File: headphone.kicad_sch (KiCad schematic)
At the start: 5 parts, among them J4 SFV14R-2STE1HLF, Q2 NTK3139PT1G

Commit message: layout, routing: relayout and reroute board
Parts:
- J4: value SFV14R-2STE1HLF -> (none); footprint Gigahawk:SFV14R2STE1HLF -> (none)
- Q2: value NTK3139PT1G -> (none); footprint Package_TO_SOT_SMD:SOT-723 -> (none)
- R28, R30: value 10k -> (none); footprint Resistor_SMD:R_0402_1005Metric -> (none)
- R29: value DNI -> (none); footprint Resistor_SMD:R_0402_1005Metric -> (none)
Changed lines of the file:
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@@
     (in_bom yes) (on_board yes) (fields_autoplaced)
     (property "Reference" "Q2" (id 0) (at 181.865 95.25 90))
-    (property "Value" "NTK3139PT1G" (id 1) (at 181.865 97.79 90))
-    (property "Footprint" "Package_TO_SOT_SMD:SOT-723" (id 2) (at 193.04 104.14 0)
+    (property "Value" "" (id 1) (at 181.865 97.79 90))
+    (property "Footprint" "" (id 2) (at 193.04 104.14 0)
       (effects (font (size 1.27 1.27)) hide)
     )
@@
     (in_bom yes) (on_board yes)
     (property "Reference" "R30" (id 0) (at 186.69 113.665 90))
-    (property "Value" "10k" (id 1) (at 186.69 115.57 90))
-    (property "Footprint" "Resistor_SMD:R_0402_1005Metric" (id 2) (at 186.69 111.76 0)
+    (property "Value" "" (id 1) (at 186.69 115.57 90))
+    (property "Footprint" "" (id 2) (at 186.69 111.76 0)
       (effects (font (size 1.27 1.27)) hide)
     )
@@
     (in_bom yes) (on_board yes) (fields_autoplaced)
     (property "Reference" "J4" (id 0) (at 119.38 93.98 0))
-    (property "Value" "SFV14R-2STE1HLF" (id 1) (at 119.38 96.52 0))
-    (property "Footprint" "Gigahawk:SFV14R2STE1HLF" (id 2) (at 127 99.06 0)
+    (property "Value" "" (id 1) (at 119.38 96.52 0))
+    (property "Footprint" "" (id 2) (at 127 99.06 0)
       (effects (font (size 1.27 1.27)) (justify left) hide)
     )
@@
     (in_bom yes) (on_board yes)
     (property "Reference" "R29" (id 0) (at 179.07 113.665 90))
-    (property "Value" "DNI" (id 1) (at 179.07 115.57 90))
-    (property "Footprint" "Resistor_SMD:R_0402_1005Metric" (id 2) (at 179.07 111.76 0)
+    (property "Value" "" (id 1) (at 179.07 115.57 90))
+    (property "Footprint" "" (id 2) (at 179.07 111.76 0)
       (effects (font (size 1.27 1.27)) hide)
     )
@@
       (effects (font (size 1.27 1.27)) (justify left))
     )
-    (property "Value" "10k" (id 1) (at 156.845 110.49 90)
-      (effects (font (size 1.27 1.27)) (justify right))
-    )
-    (property "Footprint" "Resistor_SMD:R_0402_1005Metric" (id 2) (at 154.94 109.22 0)
-      (effects (font (size 1.27 1.27)) hide)
-    )
+    (property "Value" "" (id 1) (at 156.845 110.49 90)
+      (effects (font (size 1.27 1.27)) (justify right))
+    )
+    (property "Footprint" "" (id 2) (at 154.94 109.22 0)
+      (effects (font (size 1.27 1.27)) hide)
+    )

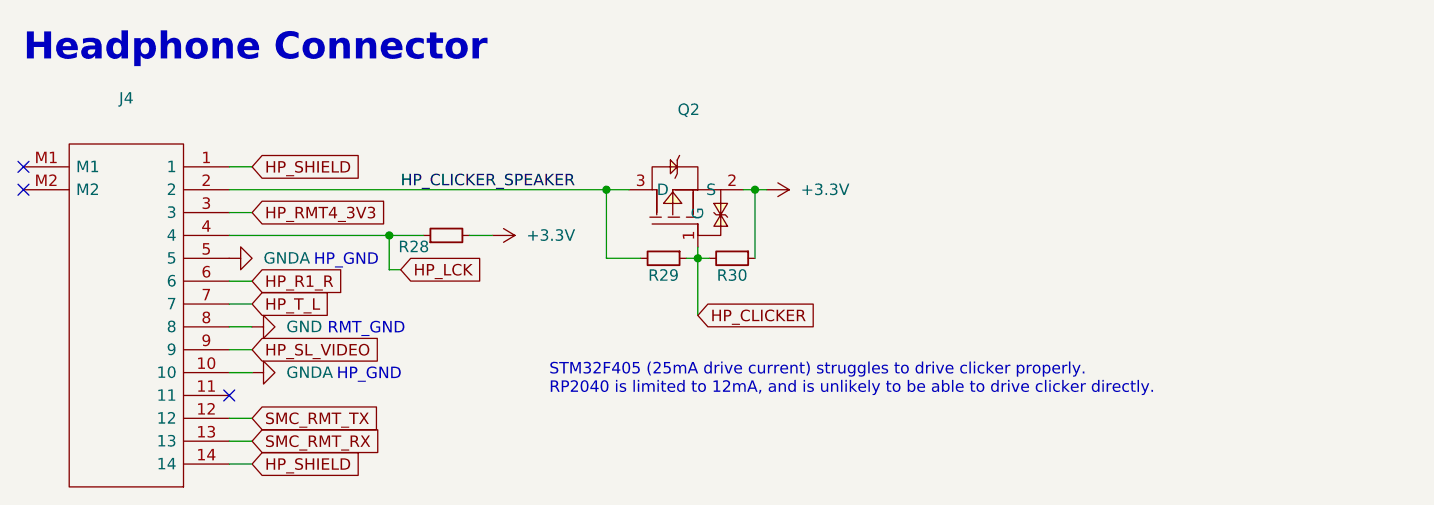
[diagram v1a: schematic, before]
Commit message: layout: add testpoints, extra mounting hole, grounding clips
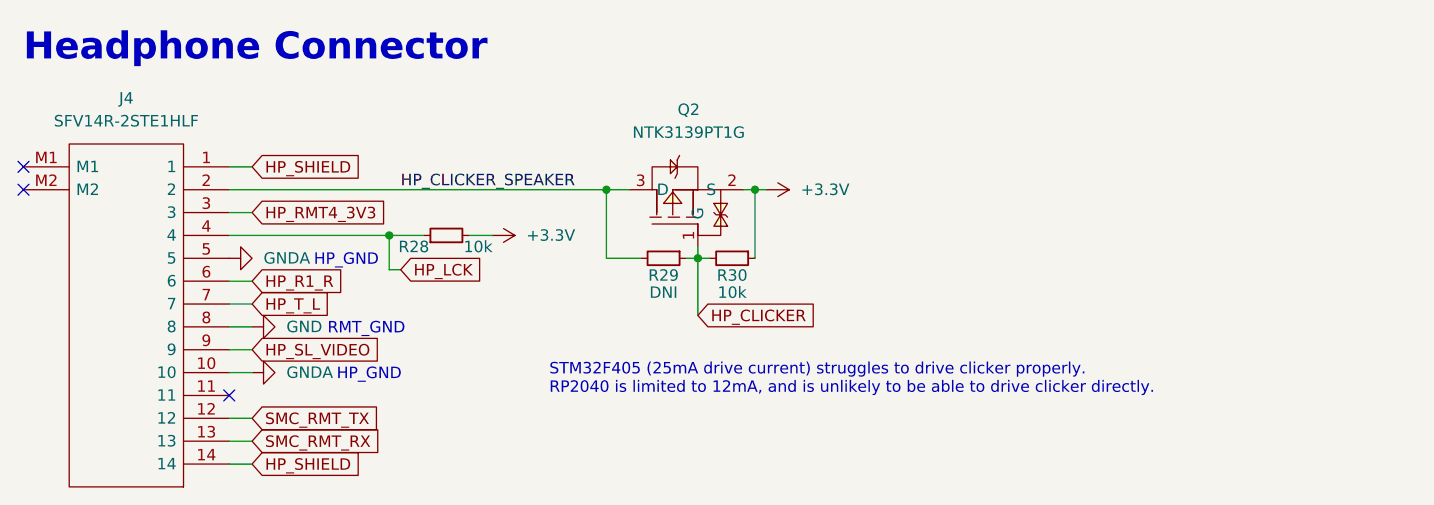
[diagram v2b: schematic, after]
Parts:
- J4: value (none) -> SFV14R-2STE1HLF; footprint (none) -> Gigahawk:SFV14R2STE1HLF
- Q2: value (none) -> NTK3139PT1G; footprint (none) -> Package_TO_SOT_SMD:SOT-723
- R28, R30: value (none) -> 10k; footprint (none) -> Resistor_SMD:R_0402_1005Metric
- R29: value (none) -> DNI; footprint (none) -> Resistor_SMD:R_0402_1005Metric
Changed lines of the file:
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@@
     (in_bom yes) (on_board yes) (fields_autoplaced)
     (property "Reference" "Q2" (id 0) (at 181.865 95.25 90))
-    (property "Value" "" (id 1) (at 181.865 97.79 90))
-    (property "Footprint" "" (id 2) (at 193.04 104.14 0)
+    (property "Value" "NTK3139PT1G" (id 1) (at 181.865 97.79 90))
+    (property "Footprint" "Package_TO_SOT_SMD:SOT-723" (id 2) (at 193.04 104.14 0)
       (effects (font (size 1.27 1.27)) hide)
     )
@@
     (in_bom yes) (on_board yes)
     (property "Reference" "R30" (id 0) (at 186.69 113.665 90))
-    (property "Value" "" (id 1) (at 186.69 115.57 90))
-    (property "Footprint" "" (id 2) (at 186.69 111.76 0)
+    (property "Value" "10k" (id 1) (at 186.69 115.57 90))
+    (property "Footprint" "Resistor_SMD:R_0402_1005Metric" (id 2) (at 186.69 111.76 0)
       (effects (font (size 1.27 1.27)) hide)
     )
@@
     (in_bom yes) (on_board yes) (fields_autoplaced)
     (property "Reference" "J4" (id 0) (at 119.38 93.98 0))
-    (property "Value" "" (id 1) (at 119.38 96.52 0))
-    (property "Footprint" "" (id 2) (at 127 99.06 0)
+    (property "Value" "SFV14R-2STE1HLF" (id 1) (at 119.38 96.52 0))
+    (property "Footprint" "Gigahawk:SFV14R2STE1HLF" (id 2) (at 127 99.06 0)
       (effects (font (size 1.27 1.27)) (justify left) hide)
     )
@@
     (in_bom yes) (on_board yes)
     (property "Reference" "R29" (id 0) (at 179.07 113.665 90))
-    (property "Value" "" (id 1) (at 179.07 115.57 90))
-    (property "Footprint" "" (id 2) (at 179.07 111.76 0)
+    (property "Value" "DNI" (id 1) (at 179.07 115.57 90))
+    (property "Footprint" "Resistor_SMD:R_0402_1005Metric" (id 2) (at 179.07 111.76 0)
       (effects (font (size 1.27 1.27)) hide)
     )
@@
       (effects (font (size 1.27 1.27)) (justify left))
     )
-    (property "Value" "" (id 1) (at 156.845 110.49 90)
-      (effects (font (size 1.27 1.27)) (justify right))
-    )
-    (property "Footprint" "" (id 2) (at 154.94 109.22 0)
-      (effects (font (size 1.27 1.27)) hide)
-    )
+    (property "Value" "10k" (id 1) (at 156.845 110.49 90)
+      (effects (font (size 1.27 1.27)) (justify right))
+    )
+    (property "Footprint" "Resistor_SMD:R_0402_1005Metric" (id 2) (at 154.94 109.22 0)
+      (effects (font (size 1.27 1.27)) hide)
+    )

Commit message: ci: prepare files for CI
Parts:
- Q2: footprint Package_TO_SOT_SMD:SOT-723 -> Gigahawk:SOT-723
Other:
- title: (none) -> piPod IO/SMC Board
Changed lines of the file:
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@@
 (kicad_sch (version 20211123) (generator eeschema)
   (paper "A4")
+  (title_block
+    (title "piPod IO/SMC Board")
+    (date "${DATE}")
+    (rev "%{TAG} (${REVISION})")
+  )
   (junction (at 148.59 109.22) (diameter 0) (color 0 0 0 0)
   )
@@
     (property "Reference" "Q2" (id 0) (at 181.865 95.25 90))
     (property "Value" "NTK3139PT1G" (id 1) (at 181.865 97.79 90))
-    (property "Footprint" "Package_TO_SOT_SMD:SOT-723" (id 2) (at 193.04 104.14 0)
+    (property "Footprint" "Gigahawk:SOT-723" (id 2) (at 193.04 104.14 0)
       (effects (font (size 1.27 1.27)) hide)
     )

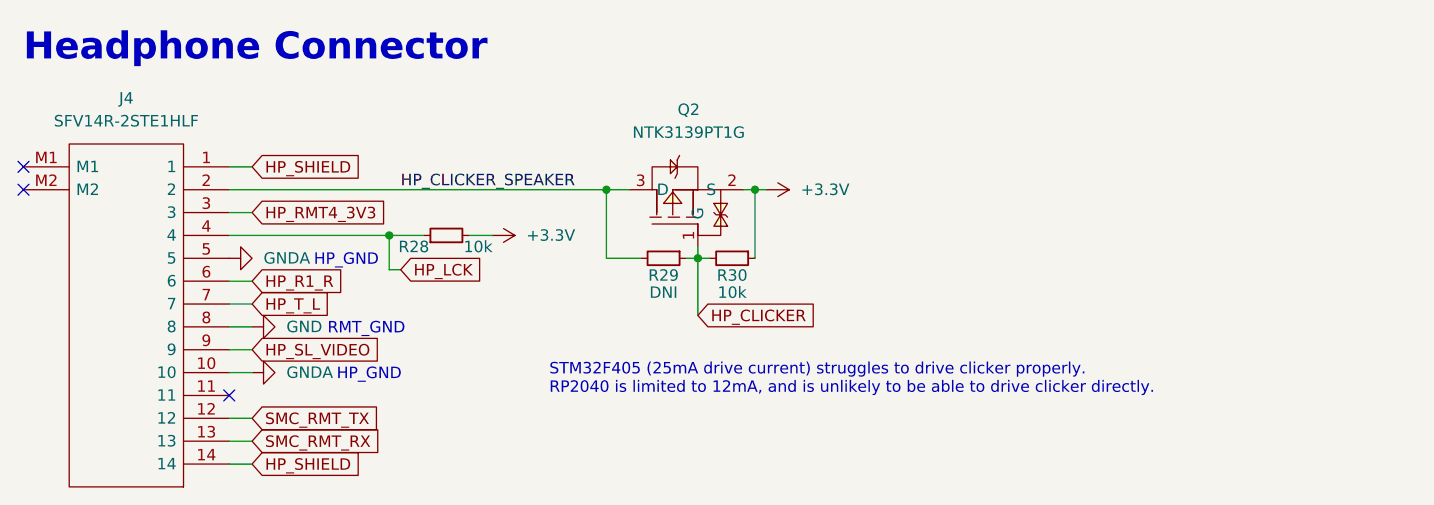
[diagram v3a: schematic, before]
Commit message: ci: test marking parts in sch for bom
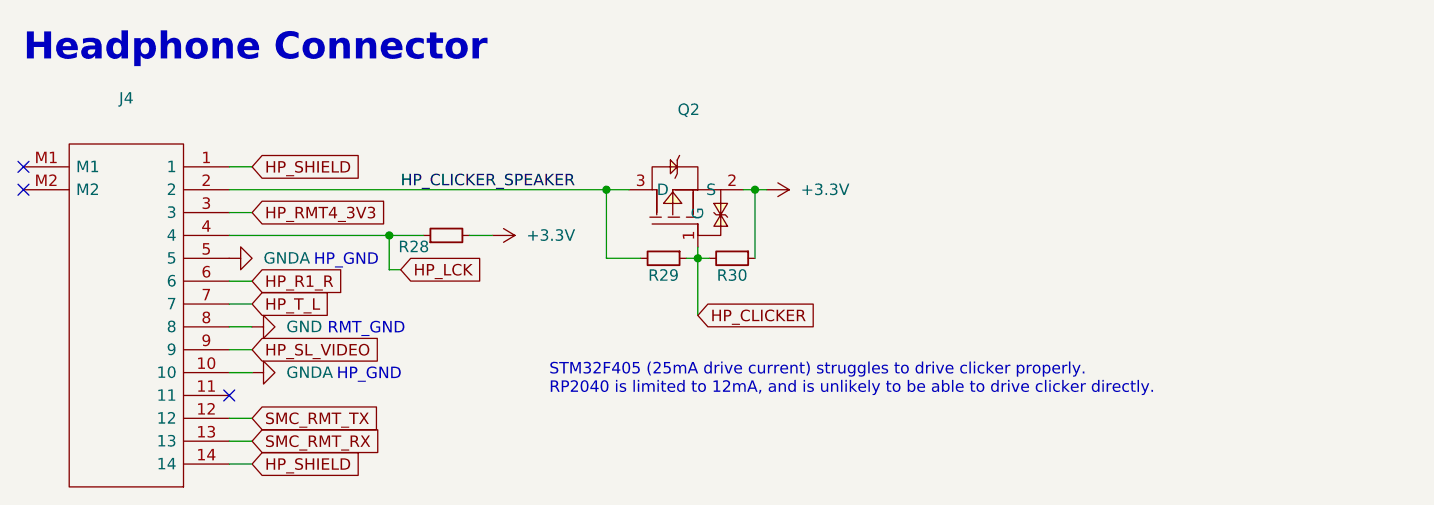
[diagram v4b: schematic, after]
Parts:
- J4: value SFV14R-2STE1HLF -> (none); footprint Gigahawk:SFV14R2STE1HLF -> (none)
- Q2: value NTK3139PT1G -> (none); footprint Gigahawk:SOT-723 -> (none)
- R28, R30: value 10k -> (none); footprint Resistor_SMD:R_0402_1005Metric -> (none)
- R29: value DNI -> (none); footprint Resistor_SMD:R_0402_1005Metric -> (none)
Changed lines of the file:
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@@
     (in_bom yes) (on_board yes) (fields_autoplaced)
     (property "Reference" "Q2" (id 0) (at 181.865 95.25 90))
-    (property "Value" "NTK3139PT1G" (id 1) (at 181.865 97.79 90))
-    (property "Footprint" "Gigahawk:SOT-723" (id 2) (at 193.04 104.14 0)
+    (property "Value" "" (id 1) (at 181.865 97.79 90))
+    (property "Footprint" "" (id 2) (at 193.04 104.14 0)
       (effects (font (size 1.27 1.27)) hide)
     )
@@
     (in_bom yes) (on_board yes)
     (property "Reference" "R30" (id 0) (at 186.69 113.665 90))
-    (property "Value" "10k" (id 1) (at 186.69 115.57 90))
-    (property "Footprint" "Resistor_SMD:R_0402_1005Metric" (id 2) (at 186.69 111.76 0)
+    (property "Value" "" (id 1) (at 186.69 115.57 90))
+    (property "Footprint" "" (id 2) (at 186.69 111.76 0)
       (effects (font (size 1.27 1.27)) hide)
     )
@@
     (in_bom yes) (on_board yes) (fields_autoplaced)
     (property "Reference" "J4" (id 0) (at 119.38 93.98 0))
-    (property "Value" "SFV14R-2STE1HLF" (id 1) (at 119.38 96.52 0))
-    (property "Footprint" "Gigahawk:SFV14R2STE1HLF" (id 2) (at 127 99.06 0)
+    (property "Value" "" (id 1) (at 119.38 96.52 0))
+    (property "Footprint" "" (id 2) (at 127 99.06 0)
       (effects (font (size 1.27 1.27)) (justify left) hide)
     )
@@
     (in_bom yes) (on_board yes)
     (property "Reference" "R29" (id 0) (at 179.07 113.665 90))
-    (property "Value" "DNI" (id 1) (at 179.07 115.57 90))
-    (property "Footprint" "Resistor_SMD:R_0402_1005Metric" (id 2) (at 179.07 111.76 0)
+    (property "Value" "" (id 1) (at 179.07 115.57 90))
+    (property "Footprint" "" (id 2) (at 179.07 111.76 0)
       (effects (font (size 1.27 1.27)) hide)
     )
@@
       (effects (font (size 1.27 1.27)) (justify left))
     )
-    (property "Value" "10k" (id 1) (at 156.845 110.49 90)
-      (effects (font (size 1.27 1.27)) (justify right))
-    )
-    (property "Footprint" "Resistor_SMD:R_0402_1005Metric" (id 2) (at 154.94 109.22 0)
-      (effects (font (size 1.27 1.27)) hide)
-    )
+    (property "Value" "" (id 1) (at 156.845 110.49 90)
+      (effects (font (size 1.27 1.27)) (justify right))
+    )
+    (property "Footprint" "" (id 2) (at 154.94 109.22 0)
+      (effects (font (size 1.27 1.27)) hide)
+    )
